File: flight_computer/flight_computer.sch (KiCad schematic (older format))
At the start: 2 parts

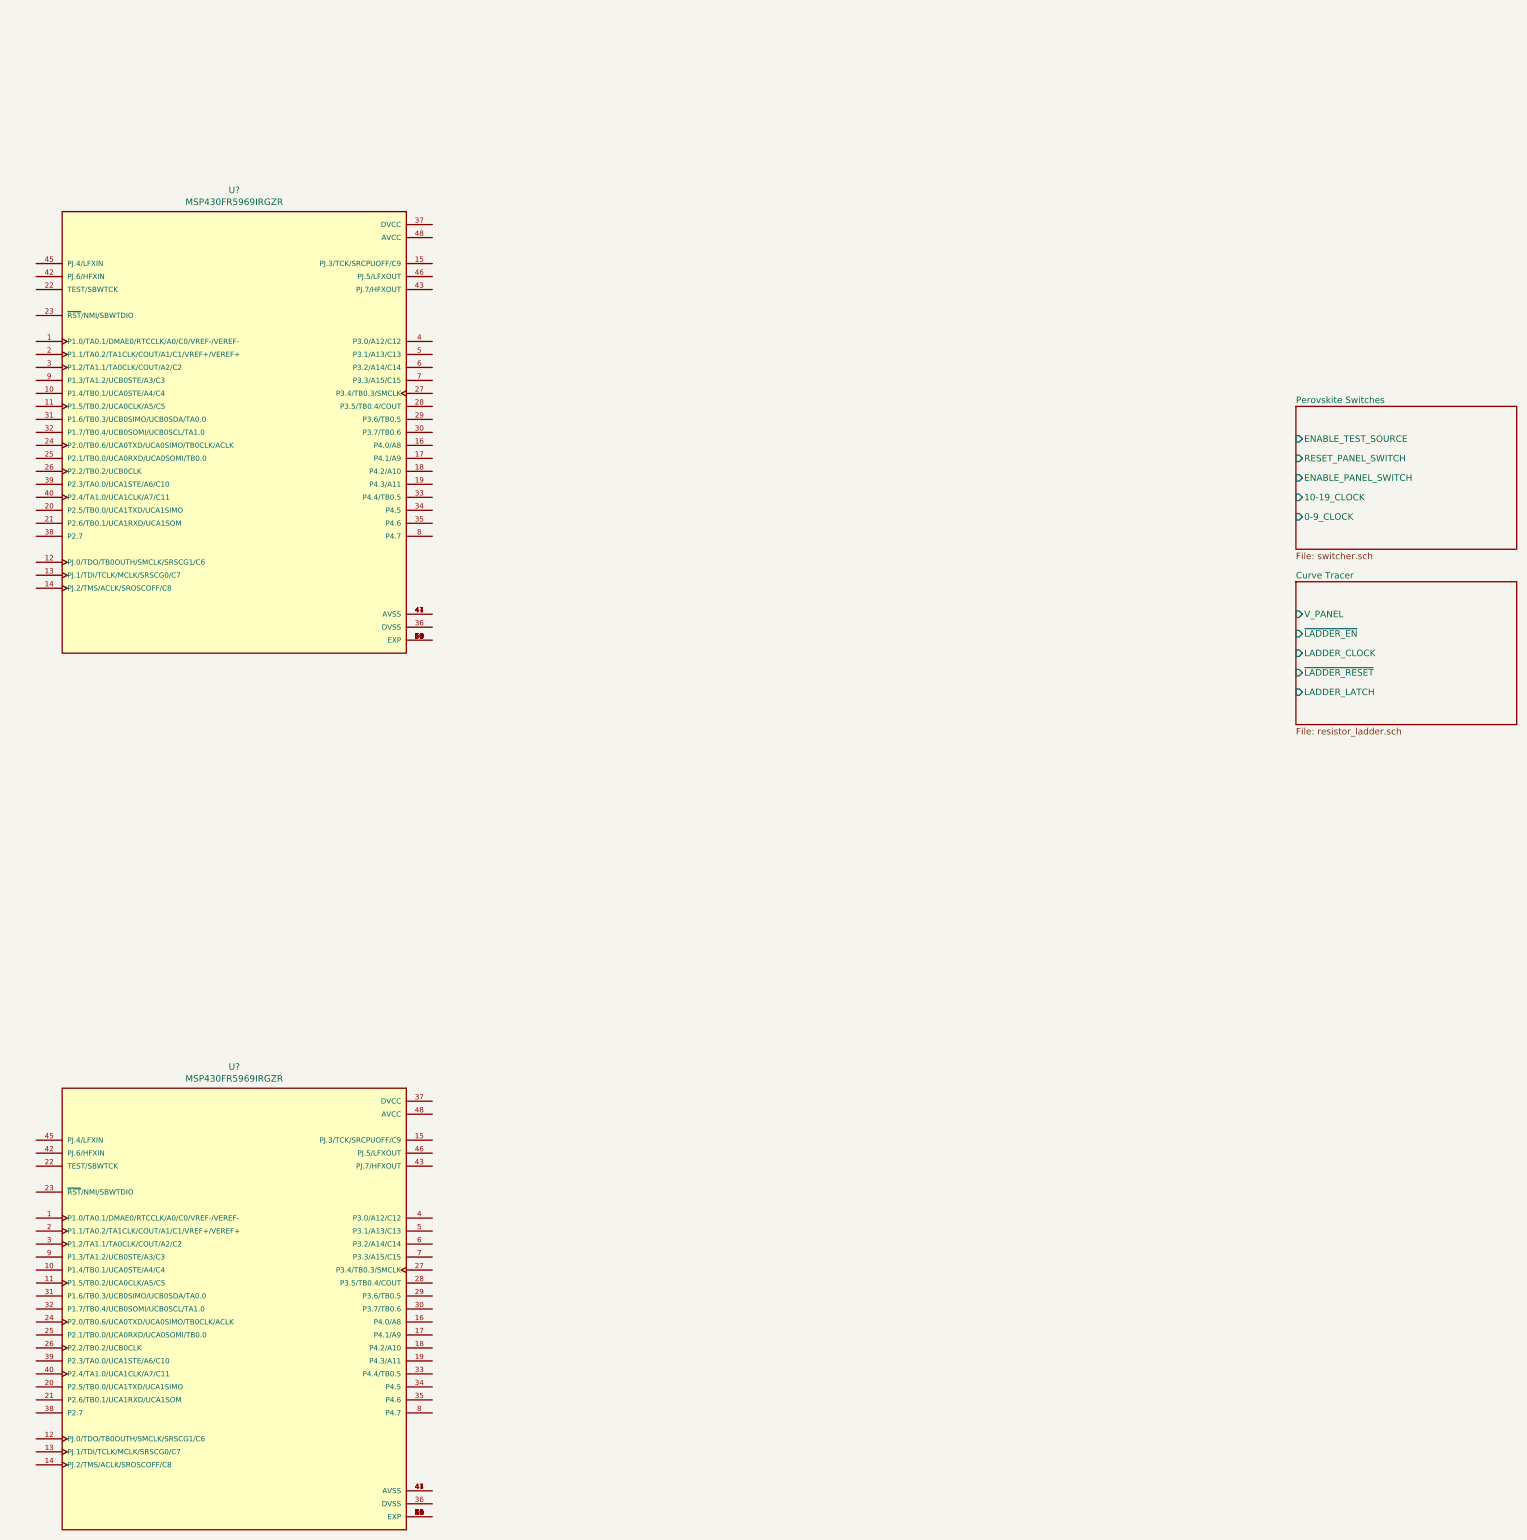
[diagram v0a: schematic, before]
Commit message: Working on flight computer
- Update resistor ladder curve tracer silkscreen, schematic, and layout
- Flight computer schematic drafted for MSP430 circuits, updated curve tracer, perovskite switching network.
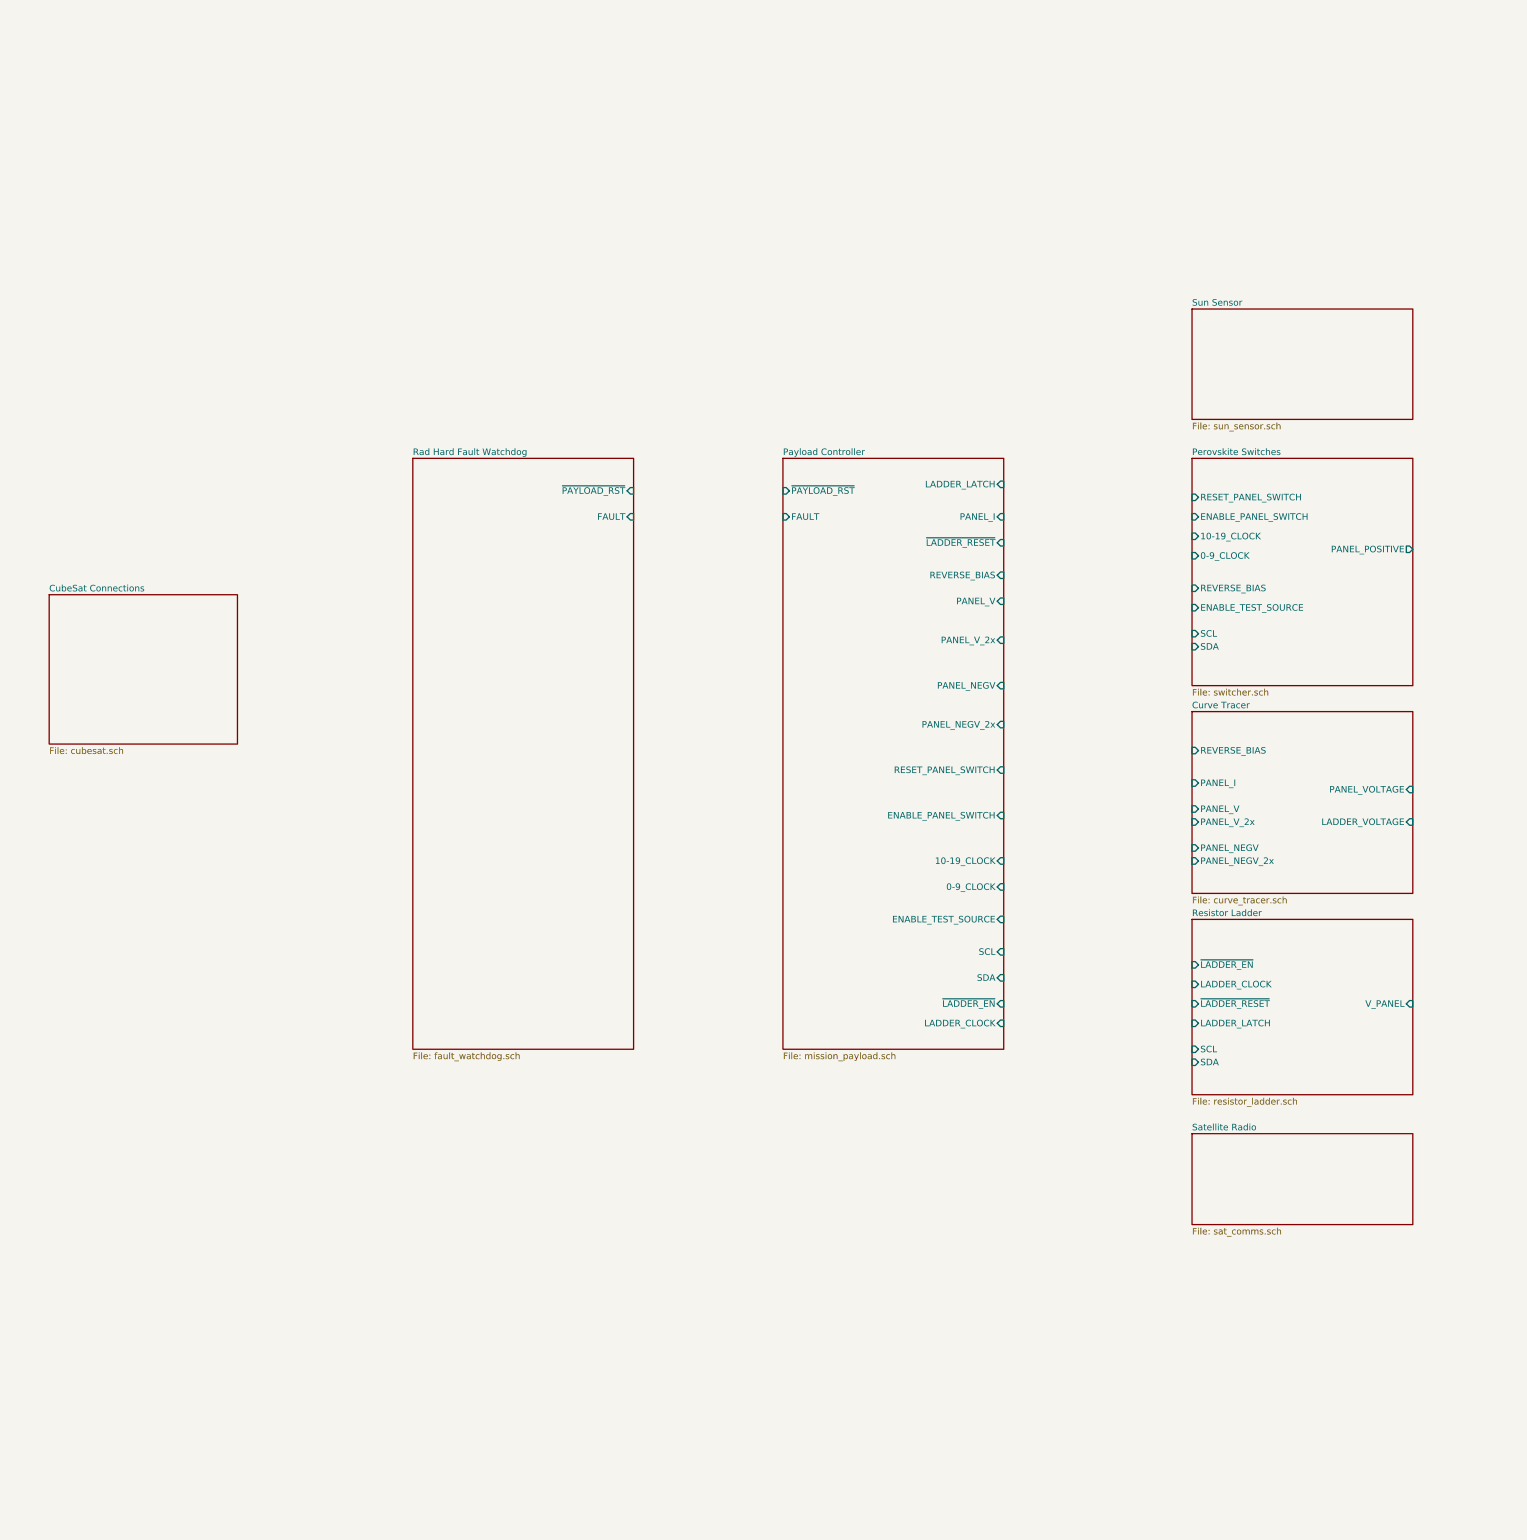
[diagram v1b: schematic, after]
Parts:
- removed U? (x2): MSP430FR5969IRGZR, QFN50P700X700X100-49N, symbol MSP430FR5969IRGZR:MSP430FR5969IRGZR
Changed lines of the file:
@@
 $Descr A2 23386 16535
 encoding utf-8
-Sheet 1 3
+Sheet 1 9
 Title ""
 Date ""
@@
 $EndDescr
 $Sheet
-S 14550 4750 1700 1100
+S 13750 8700 1700 1350
+U 635FEB2F
+F0 "Resistor Ladder" 50
+F1 "resistor_ladder.sch" 50
+F2 "V_PANEL" I R 15450 9350 50
+F3 "~LADDER_EN" I L 13750 9050 50
+F4 "LADDER_CLOCK" I L 13750 9200 50
+F5 "~LADDER_RESET" I L 13750 9350 50
+F6 "LADDER_LATCH" I L 13750 9500 50
+F7 "SCL" I L 13750 9700 50
+F8 "SDA" I L 13750 9800 50
+$EndSheet
+$Sheet
+S 13750 7100 1700 1400
+U 63C503EE
+F0 "Curve Tracer" 50
+F1 "curve_tracer.sch" 50
+F2 "PANEL_VOLTAGE" I R 15450 7700 50
+F3 "LADDER_VOLTAGE" I R 15450 7950 50
+F4 "PANEL_V" I L 13750 7850 50
+F5 "PANEL_I" I L 13750 7650 50
+F6 "PANEL_V_2x" I L 13750 7950 50
+F7 "REVERSE_BIAS" I L 13750 7400 50
+F8 "PANEL_NEGV" I L 13750 8150 50
+F9 "PANEL_NEGV_2x" I L 13750 8250 50
+$EndSheet
+$Sheet
+S 13750 5150 1700 1750
 U 635FE71D
 F0 "Perovskite Switches" 50
 F1 "switcher.sch" 50
-F2 "ENABLE_TEST_SOURCE" I L 14550 5000 50
-F3 "RESET_PANEL_SWITCH" I L 14550 5150 50
-F4 "ENABLE_PANEL_SWITCH" I L 14550 5300 50
-F5 "10-19_CLOCK" I L 14550 5450 50
-F6 "0-9_CLOCK" I L 14550 5600 50
+F2 "ENABLE_TEST_SOURCE" I L 13750 6300 50
+F3 "RESET_PANEL_SWITCH" I L 13750 5450 50
+F4 "ENABLE_PANEL_SWITCH" I L 13750 5600 50
+F5 "10-19_CLOCK" I L 13750 5750 50
+F6 "0-9_CLOCK" I L 13750 5900 50
+F7 "PANEL_POSITIVE" O R 15450 5850 50
+F8 "REVERSE_BIAS" I L 13750 6150 50
+F9 "SDA" I L 13750 6600 50
+F10 "SCL" I L 13750 6500 50
 $EndSheet
 $Sheet
-S 14550 6100 1700 1100
-U 635FEB2F
-F0 "Curve Tracer" 50
-F1 "resistor_ladder.sch" 50
-F2 "V_PANEL" I L 14550 6350 50
-F3 "~LADDER_EN" I L 14550 6500 50
-F4 "LADDER_CLOCK" I L 14550 6650 50
-F5 "~LADDER_RESET" I L 14550 6800 50
-F6 "LADDER_LATCH" I L 14550 6950 50
+S 7750 5150 1700 4550
+U 63D1F518
+F0 "Rad Hard Fault Watchdog" 50
+F1 "fault_watchdog.sch" 50
+F2 "FAULT" I R 9450 5600 50
+F3 "~PAYLOAD_RST" I R 9450 5400 50
 $EndSheet
-$Comp
-L MSP430FR5969IRGZR:MSP430FR5969IRGZR U?
-U 1 1 63602BA6
-P 6400 11700
-F 0 "U?" H 6375 13565 50  0000 C CNN
-F 1 "MSP430FR5969IRGZR" H 6375 13474 50  0000 C CNN
-F 2 "QFN50P700X700X100-49N" H 6800 11700 50  0001 L BNN
-F 3 "" H 6800 11700 50  0001 L BNN
-	1    6400 11700
-	1    0    0    -1
-$EndComp
-$Comp
-L MSP430FR5969IRGZR:MSP430FR5969IRGZR U?
-U 1 1 6360462F
-P 6400 4950
-F 0 "U?" H 6375 6815 50  0000 C CNN
-F 1 "MSP430FR5969IRGZR" H 6375 6724 50  0000 C CNN
-F 2 "QFN50P700X700X100-49N" H 6800 4950 50  0001 L BNN
-F 3 "" H 6800 4950 50  0001 L BNN
-	1    6400 4950
-	1    0    0    -1
-$EndComp
+$Sheet
+S 10600 5150 1700 4550
+U 63D21EEE
+F0 "Payload Controller" 50
+F1 "mission_payload.sch" 50
+F2 "PANEL_I" I R 12300 5600 50
+F3 "REVERSE_BIAS" I R 12300 6050 50
+F4 "PANEL_V" I R 12300 6250 50
+F5 "PANEL_V_2x" I R 12300 6550 50
+F6 "PANEL_NEGV" I R 12300 6900 50
+F7 "PANEL_NEGV_2x" I R 12300 7200 50
+F8 "RESET_PANEL_SWITCH" I R 12300 7550 50
+F9 "ENABLE_PANEL_SWITCH" I R 12300 7900 50
+F10 "10-19_CLOCK" I R 12300 8250 50
+F11 "0-9_CLOCK" I R 12300 8450 50
+F12 "ENABLE_TEST_SOURCE" I R 12300 8700 50
+F13 "SCL" I R 12300 8950 50
+F14 "SDA" I R 12300 9150 50
+F15 "~LADDER_EN" I R 12300 9350 50
+F16 "LADDER_CLOCK" I R 12300 9500 50
+F17 "~LADDER_RESET" I R 12300 5800 50
+F18 "LADDER_LATCH" I R 12300 5350 50
+F19 "~PAYLOAD_RST" I L 10600 5400 50
+F20 "FAULT" I L 10600 5600 50
+$EndSheet
+$Sheet
+S 4950 6200 1450 1150
+U 63D2A1A8
+F0 "CubeSat Connections" 50
+F1 "cubesat.sch" 50
+$EndSheet
+$Sheet
+S 13750 4000 1700 850
+U 63D2A1C8
+F0 "Sun Sensor" 50
+F1 "sun_sensor.sch" 50
+$EndSheet
+$Sheet
+S 13750 10350 1700 700
+U 63D2A1FC
+F0 "Satellite Radio" 50
+F1 "sat_comms.sch" 50
+$EndSheet
 $EndSCHEMATC

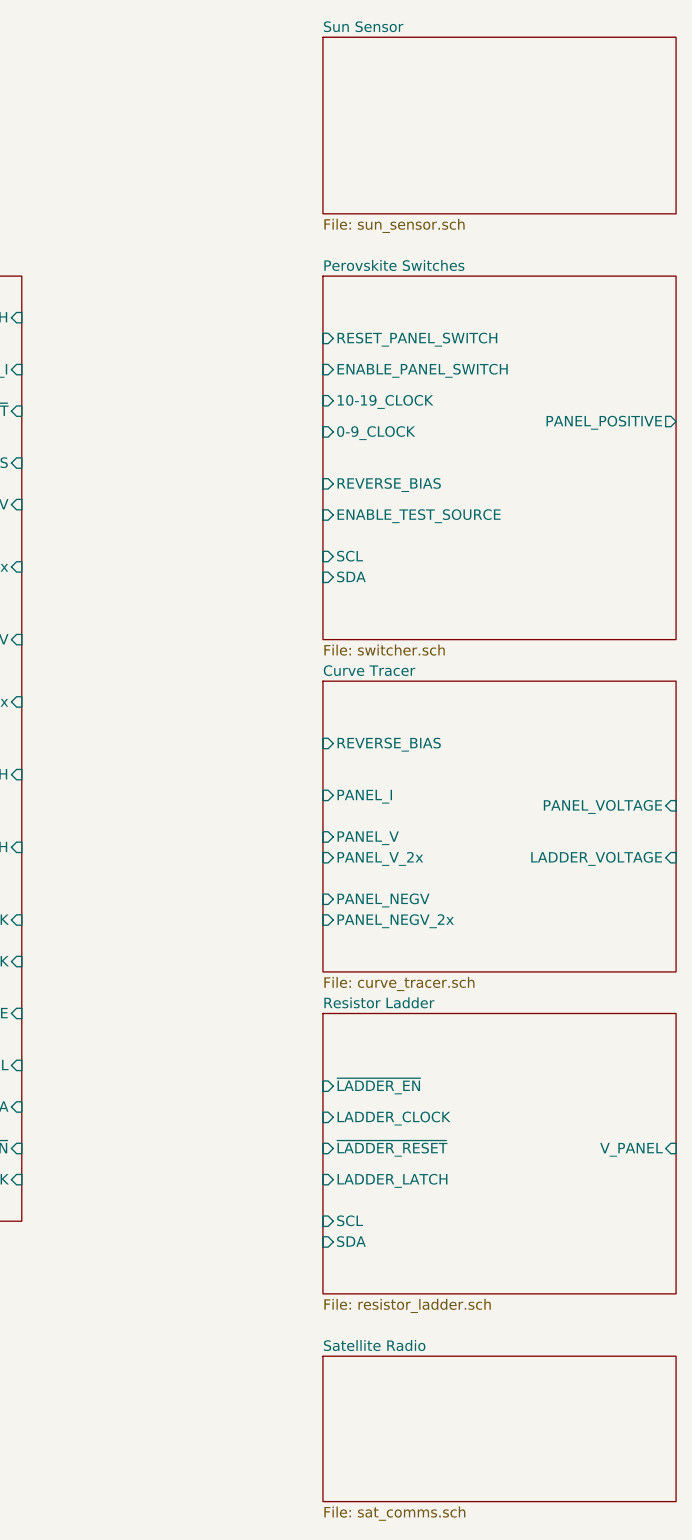
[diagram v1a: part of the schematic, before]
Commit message: Updating flight computer
- Added datasheets for peripherals
- Added resistor ladder firmware
- Added perovskite switcher firmware
- Started flight computer firmware
- Added curve comparisons
- Updating flight computer schematic
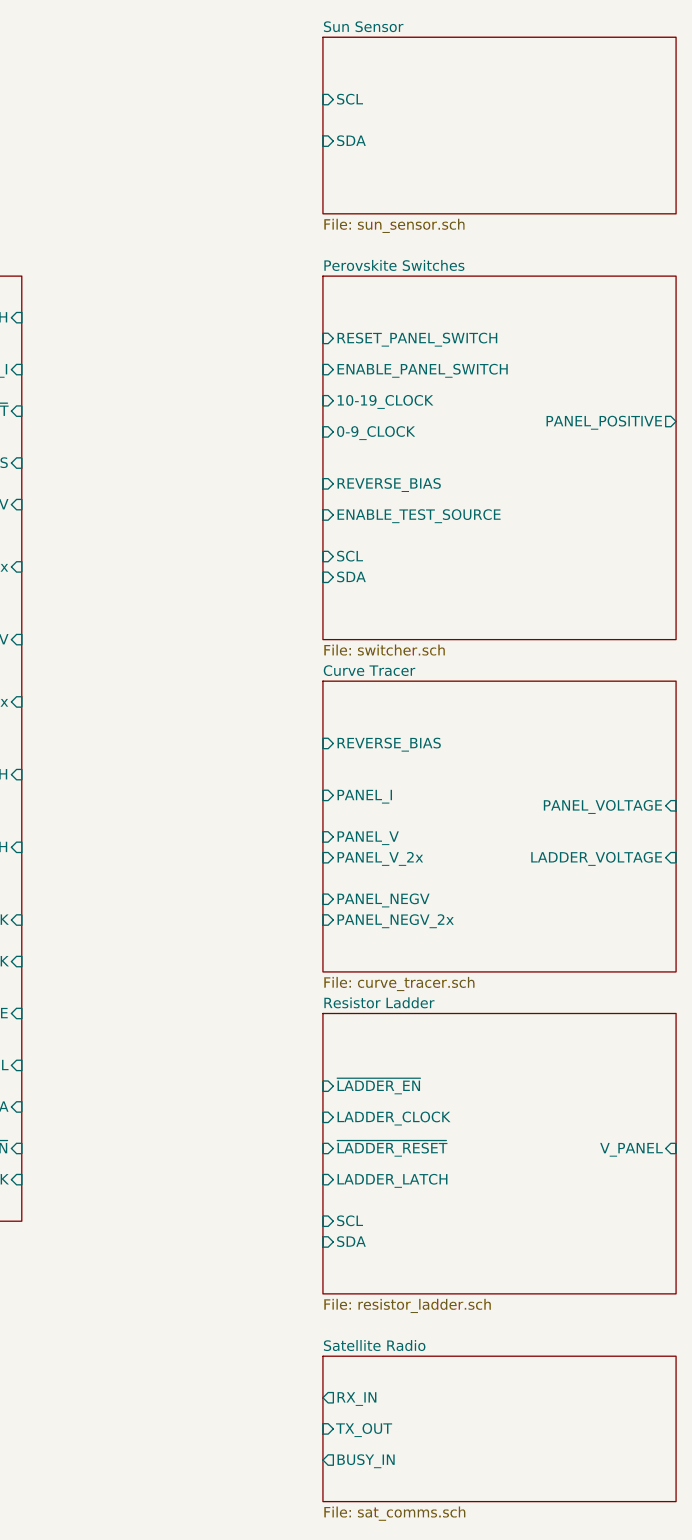
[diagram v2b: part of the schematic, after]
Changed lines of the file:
@@
 F0 "Sun Sensor" 50
 F1 "sun_sensor.sch" 50
+F2 "SCL" I L 13750 4300 50
+F3 "SDA" I L 13750 4500 50
 $EndSheet
 $Sheet
@@
 F0 "Satellite Radio" 50
 F1 "sat_comms.sch" 50
+F2 "RX_IN" O L 13750 10550 50
+F3 "TX_OUT" I L 13750 10700 50
+F4 "BUSY_IN" O L 13750 10850 50
 $EndSheet
 $EndSCHEMATC
